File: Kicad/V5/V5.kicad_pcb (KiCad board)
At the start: 2 copper layers, 88.9 x 119.4 mm, 40 parts, among them J1 Conn_01x02_Pin, J2 Conn_01x02_Pin, J3 Conn_01x02_Pin, J4 Conn_01x02_Pin, J5 Conn_01x02_Pin, J6 Conn_01x02_Pin, U1 ISOM8600DFGR, U10 ISOM8600DFGR, U11 ISOM8600DFGR, U12 ISOM8600DFGR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

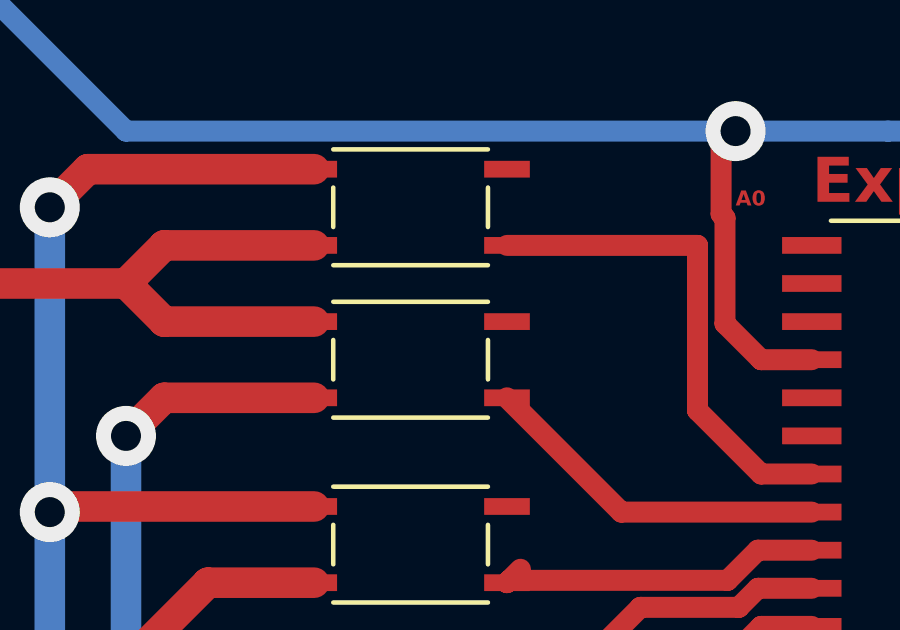
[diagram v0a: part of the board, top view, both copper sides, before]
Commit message: ajout du projet salle blanche et pcb capteur fini
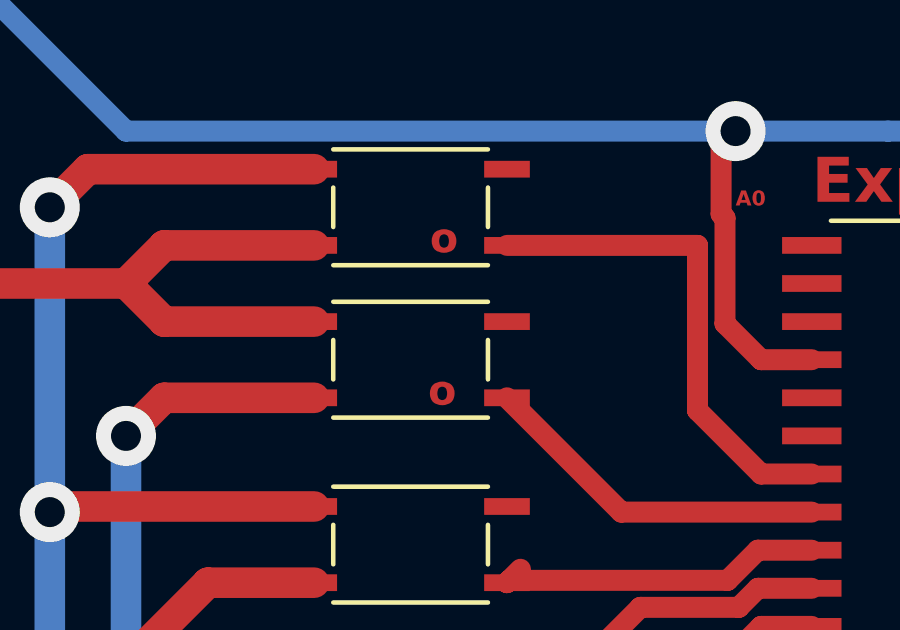
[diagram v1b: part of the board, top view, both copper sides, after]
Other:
- board text added: "ISOM86"
- board text added: "MCP23017 (composant boite noire)"
- board text added: "MIC5283"
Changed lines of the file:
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@@
     (pad "10" smd rect (at 2.21615 -1.000252 270) (size 1.3335 0.2794) (layers "F.Cu" "F.Paste" "F.Mask")
       (net 16 "Net-(U7-IN+)") (pinfunction "IN+") (pintype "input"))
+    (model "/home/xoum/Téléchargements/INA237AIDGSR/KiCAD/2026-04-27_21-40-41.lib" hide
+      (offset (xyz 0 0 0))
+      (scale (xyz 1 1 1))
+      (rotate (xyz 0 0 0))
+    )
+    (model "/home/xoum/Téléchargements/ESP32_Footprints/INA237.stp"
+      (offset (xyz 0 0 0))
+      (scale (xyz 1 1 1))
+      (rotate (xyz 90 180 -90))
+    )
   )
   (footprint "Resistor_THT:R_Axial_DIN0207_L6.3mm_D2.5mm_P5.08mm_Vertical" (layer "F.Cu")
@@
     (pad "4" smd rect (at 3.2131 -1.27 180) (size 1.524 0.5588) (layers "F.Cu" "F.Paste" "F.Mask")
       (net 1 "Net-(BT1-+)") (pinfunction "S1") (pintype "bidirectional"))
+    (model "/home/xoum/Téléchargements/ESP32_Footprints/DFG0004A.stp"
+      (offset (xyz 0 0 0))
+      (scale (xyz 1 1 1))
+      (rotate (xyz 0 0 0))
+    )
   )
   (footprint "Connector_PinHeader_2.54mm:PinHeader_1x02_P2.54mm_Vertical" (layer "F.Cu")
@@
     (pad "4" smd rect (at 3.2131 -1.27 180) (size 1.524 0.5588) (layers "F.Cu" "F.Paste" "F.Mask")
       (net 5 "Net-(BT4-+)") (pinfunction "S1") (pintype "bidirectional"))
+    (model "/home/xoum/Téléchargements/ESP32_Footprints/DFG0004A.stp"
+      (offset (xyz 0 0 0))
+      (scale (xyz 1 1 1))
+      (rotate (xyz 0 0 0))
+    )
   )
   (footprint "Resistor_THT:R_Axial_DIN0207_L6.3mm_D2.5mm_P5.08mm_Vertical" (layer "F.Cu")
@@
     (pad "4" smd rect (at 3.2131 -1.27 180) (size 1.524 0.5588) (layers "F.Cu" "F.Paste" "F.Mask")
       (net 11 "VIN_LDO") (pinfunction "S1") (pintype "bidirectional"))
+    (model "/home/xoum/Téléchargements/ESP32_Footprints/DFG0004A.stp"
+      (offset (xyz 0 0 0))
+      (scale (xyz 1 1 1))
+      (rotate (xyz 0 0 0))
+    )
   )
   (footprint "Connector_PinHeader_2.54mm:PinHeader_1x02_P2.54mm_Vertical" (layer "F.Cu")
@@
     (pad "4" smd rect (at 3.2131 -1.27 180) (size 1.524 0.5588) (layers "F.Cu" "F.Paste" "F.Mask")
       (net 20 "V_BUS") (pinfunction "S1") (pintype "bidirectional"))
+    (model "/home/xoum/Téléchargements/ESP32_Footprints/DFG0004A.stp"
+      (offset (xyz 0 0 0))
+      (scale (xyz 1 1 1))
+      (rotate (xyz 0 0 0))
+    )
   )
   (footprint "Connector_PinHeader_2.54mm:PinHeader_1x02_P2.54mm_Vertical" (layer "F.Cu")
@@
     (pad "4" smd rect (at 3.2131 -1.27 180) (size 1.524 0.5588) (layers "F.Cu" "F.Paste" "F.Mask")
       (net 20 "V_BUS") (pinfunction "S1") (pintype "bidirectional"))
+    (model "/home/xoum/Téléchargements/ESP32_Footprints/DFG0004A.stp"
+      (offset (xyz 0 0 0))
+      (scale (xyz 1 1 1))
+      (rotate (xyz 0 0 0))
+    )
   )
   (footprint "footprints:MCP23017T-E&slash_SO" (layer "F.Cu")
@@
     (pad "28" smd rect (at 4.515 -8.255 180) (size 1.9812 0.5588) (layers "F.Cu" "F.Paste" "F.Mask")
       (net 21 "CONT_ALIM1") (pinfunction "GPA7") (pintype "bidirectional"))
+    (model "/home/xoum/Téléchargements/ESP32_Footprints/SOIC28-W_MC_MCH.step"
+      (offset (xyz 0 0 0))
+      (scale (xyz 1 1 1))
+      (rotate (xyz 0 0 0))
+    )
   )
   (footprint "footprints:ISOM8600DFGR" (layer "F.Cu")
@@
     (pad "4" smd rect (at 3.2131 -1.27 180) (size 1.524 0.5588) (layers "F.Cu" "F.Paste" "F.Mask")
       (net 20 "V_BUS") (pinfunction "S1") (pintype "bidirectional"))
+    (model "/home/xoum/Téléchargements/ESP32_Footprints/DFG0004A.stp"
+      (offset (xyz 0 0 0))
+      (scale (xyz 1 1 1))
+      (rotate (xyz 0 0 0))
+    )
   )
   (footprint "Resistor_THT:R_Axial_DIN0207_L6.3mm_D2.5mm_P5.08mm_Vertical" (layer "F.Cu")
@@
     (pad "4" smd rect (at 3.2131 -1.27 270) (size 1.524 0.5588) (layers "F.Cu" "F.Paste" "F.Mask")
       (net 17 "Net-(U4-S1)") (pinfunction "S1") (pintype "bidirectional"))
+    (model "/home/xoum/Téléchargements/ESP32_Footprints/DFG0004A.stp"
+      (offset (xyz 0 0 0))
+      (scale (xyz 1 1 1))
+      (rotate (xyz 0 0 0))
+    )
   )
   (footprint "footprints:ISOM8600DFGR" (layer "F.Cu")
@@
     (pad "4" smd rect (at 3.2131 -1.27 180) (size 1.524 0.5588) (layers "F.Cu" "F.Paste" "F.Mask")
       (net 4 "Net-(BT3-+)") (pinfunction "S1") (pintype "bidirectional"))
+    (model "/home/xoum/Téléchargements/ESP32_Footprints/DFG0004A.stp"
+      (offset (xyz 0 0 0))
+      (scale (xyz 1 1 1))
+      (rotate (xyz 0 0 0))
+    )
   )
   (footprint "Connector_PinHeader_2.54mm:PinHeader_1x02_P2.54mm_Vertical" (layer "F.Cu")
@@
     (fp_arc (start 0.3048 -2.5019) (mid 0 -2.1971) (end -0.3048 -2.5019)
       (stroke (width 0.1524) (type solid)) (layer "F.Fab"))
+    (pad "" smd rect (at 0 0 90) (size 2.413 3.0988) (layers "F.Cu" "F.Paste" "F.Mask")
+      (net 2 "GND") (pinfunction "GND") (pintype "power_in"))
     (pad "1" smd rect (at -2.72415 -1.905 90) (size 1.4605 0.5334) (layers "F.Cu" "F.Paste" "F.Mask")
       (net 11 "VIN_LDO") (pinfunction "VIN") (pintype "power_out"))
@@
     (pad "8" smd rect (at 2.72415 -1.905 90) (size 1.4605 0.5334) (layers "F.Cu" "F.Paste" "F.Mask")
       (net 10 "+3.3V") (pinfunction "VOUT") (pintype "power_in"))
-    (pad "EPAD" smd rect (at 0 0 90) (size 2.413 3.0988) (layers "F.Cu" "F.Paste" "F.Mask")
-      (net 2 "GND") (pinfunction "GND") (pintype "power_in"))
+    (model "/home/xoum/Téléchargements/ESP32_Footprints/SOIC8_EPAD_ME_MCH.step"
+      (offset (xyz 0 0 0))
+      (scale (xyz 1 1 1))
+      (rotate (xyz 0 0 0))
+    )
   )
   (footprint "Resistor_THT:R_Axial_DIN0207_L6.3mm_D2.5mm_P5.08mm_Vertical" (layer "F.Cu")
@@
     (pad "4" smd rect (at 3.2131 -1.27 180) (size 1.524 0.5588) (layers "F.Cu" "F.Paste" "F.Mask")
       (net 3 "Net-(BT2-+)") (pinfunction "S1") (pintype "bidirectional"))
+    (model "/home/xoum/Téléchargements/ESP32_Footprints/DFG0004A.stp"
+      (offset (xyz 0 0 0))
+      (scale (xyz 1 1 1))
+      (rotate (xyz 0 0 0))
+    )
   )
   (footprint "Resistor_THT:R_Axial_DIN0207_L6.3mm_D2.5mm_P5.08mm_Vertical" (layer "F.Cu")
@@
     (effects (font (size 0.5 0.5) (thickness 0.125) bold) (justify left bottom))
   )
+  (gr_text "o" (at 63.41 93.06) (layer "F.Cu")
+    (effects (font (size 1 1) (thickness 0.2) bold) (justify left bottom))
+  )
   (gr_text "Temps base" (at 40.64 35.56 90) (layer "F.Cu")
     (effects (font (size 1 1) (thickness 0.125) bold) (justify left bottom))
@@
     (effects (font (size 1 1) (thickness 0.125) bold) (justify left bottom))
   )
+  (gr_text "o" (at 63.47 87.98) (layer "F.Cu")
+    (effects (font (size 1 1) (thickness 0.2) bold) (justify left bottom))
+  )
   (gr_text "INA237" (at 101.6 119.38 90) (layer "F.Cu")
     (effects (font (size 1.3 1.3) (thickness 0.3) bold) (justify left bottom))
@@
     (effects (font (size 1 1) (thickness 0.25) bold) (justify left bottom mirror))
   )
+  (gr_text "o" (at 63.57 127.25) (layer "F.Paste")
+    (effects (font (size 1 1) (thickness 0.2) bold) (justify left bottom))
+  )
+  (gr_text "ISOM86 \n" (at 59.55 82.98) (layer "F.Paste")
+    (effects (font (size 1.5 1.5) (thickness 0.3) bold) (justify left bottom))
+  )
+  (gr_text "o" (at 81.71 104.53) (layer "F.Paste")
+    (effects (font (size 1.5 1.5) (thickness 0.2) bold) (justify left bottom))
+  )
+  (gr_text "o" (at 63.41 99.25) (layer "F.Paste")
+    (effects (font (size 1 1) (thickness 0.2) bold) (justify left bottom))
+  )
+  (gr_text "MIC5283" (at 115.78 119.27 90) (layer "F.Paste")
+    (effects (font (size 1.5 1.5) (thickness 0.3) bold) (justify left bottom))
+  )
+  (gr_text "o" (at 63.28 111.81) (layer "F.Paste")
+    (effects (font (size 1 1) (thickness 0.2) bold) (justify left bottom))
+  )
+  (gr_text "o" (at 84.33 116.29) (layer "F.Paste")
+    (effects (font (size 1 1) (thickness 0.2) bold) (justify left bottom))
+  )
+  (gr_text "ISOM86" (at 80.73 120.55 90) (layer "F.Paste")
+    (effects (font (size 1.5 1.5) (thickness 0.3) bold) (justify left bottom))
+  )
+  (gr_text "o" (at 63.7 122.27) (layer "F.Paste")
+    (effects (font (size 1 1) (thickness 0.2) bold) (justify left bottom))
+  )
+  (gr_text "o" (at 63.48 116.94) (layer "F.Paste")
+    (effects (font (size 1 1) (thickness 0.2) bold) (justify left bottom))
+  )
+  (gr_text "MCP23017 (composant boite noire)" (at 75.17 82.84) (layer "F.Paste")
+    (effects (font (size 1.5 1.5) (thickness 0.3) bold) (justify left bottom))
+  )
+  (gr_text "o" (at 63.1 104.38) (layer "F.Paste")
+    (effects (font (size 1 1) (thickness 0.2) bold) (justify left bottom))
+  )
   (segment (start 55.88 124.46) (end 53.34 121.92) (width 1.02) (layer "F.Cu") (net 1))
